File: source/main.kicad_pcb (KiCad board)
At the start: 4 copper layers, 45 x 20 mm, 34 parts, among them J1 SFPEdgeConnector, U1 SNx4LVC541A, U2 EEPROM, U3 LDO 3.3V 250mA Vin max 4.75V 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, U4 CBM9002A_56ILG

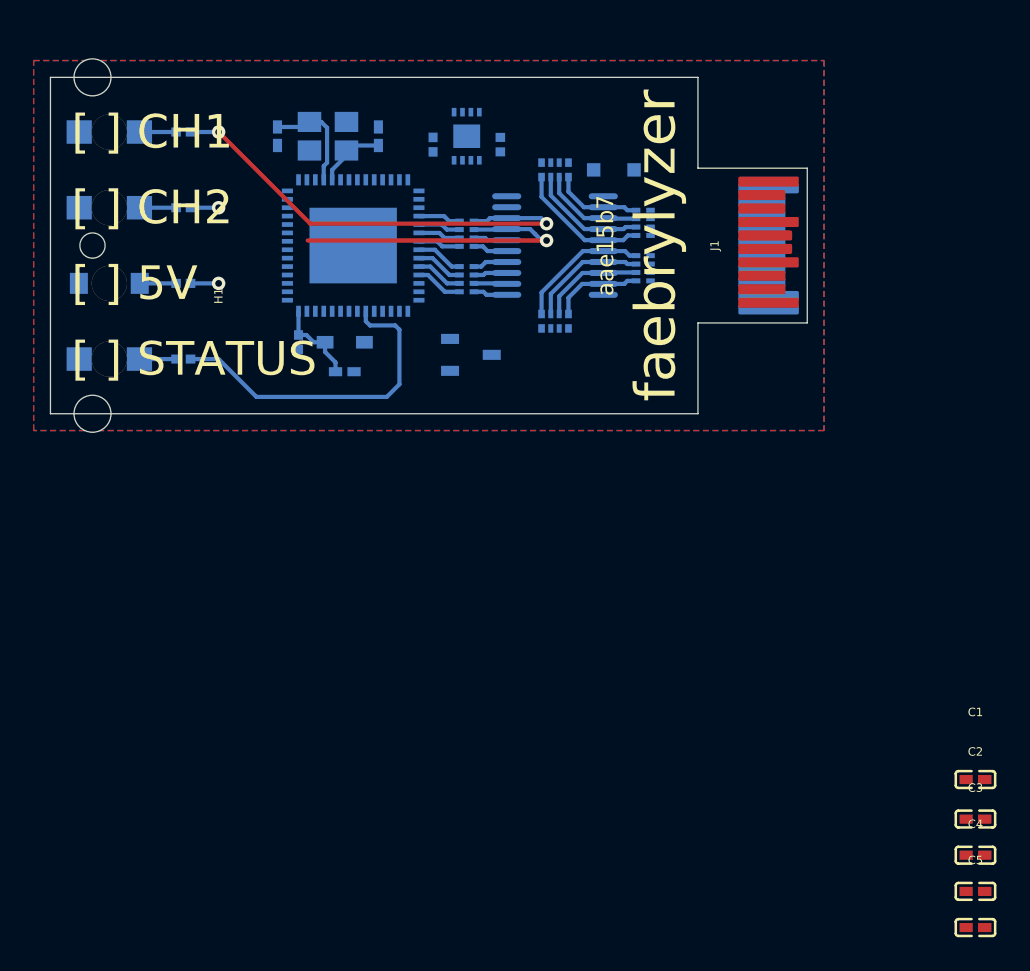
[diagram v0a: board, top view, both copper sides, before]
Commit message: Add: routing and finilize placement
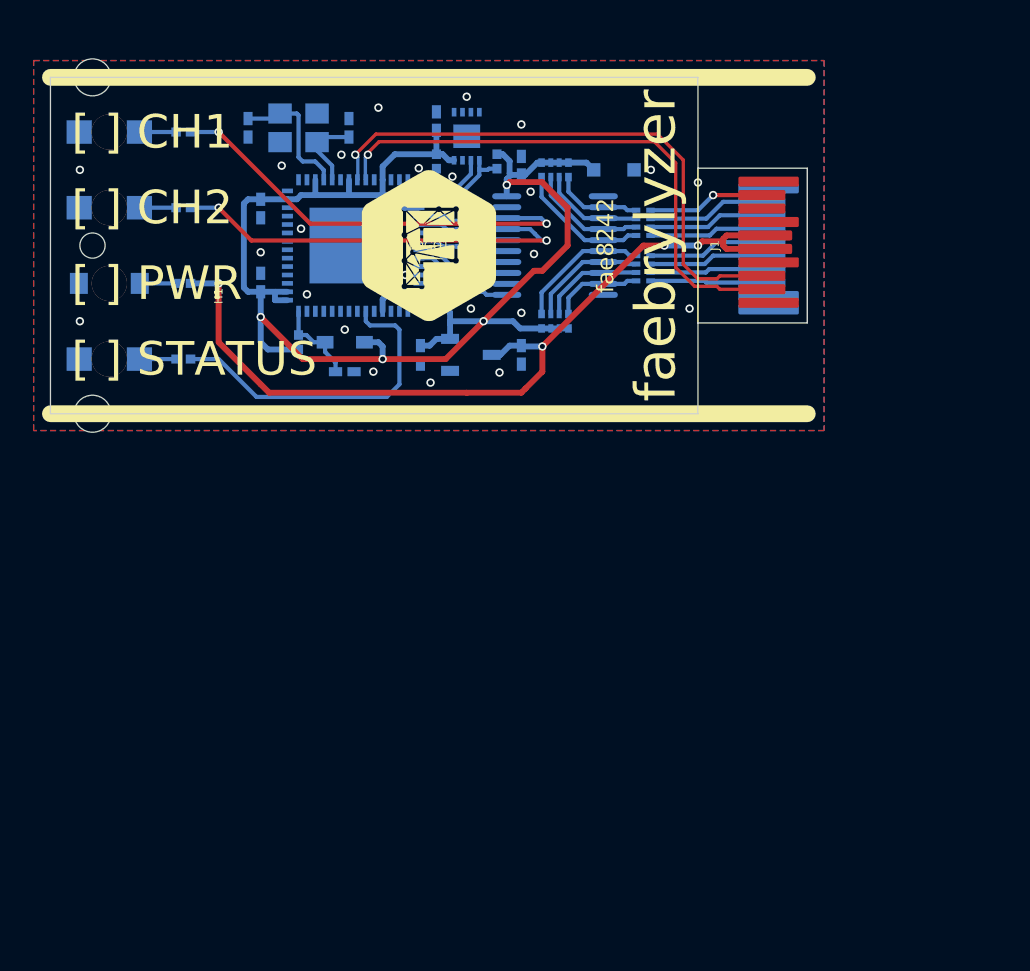
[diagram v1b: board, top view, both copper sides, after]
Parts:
- added C9: 2.2µF ±20% 6.3V X5R, lcsc:C0402, B.Cu at (28.0, 5.25)
- added LOGO1: faebrykLogo, custom:faebryk_logo, F.Cu at (22.5, 10.0)
- C1, C2, C3, C4, C5: moved to B.Cu
- moved C4 58.8 mm to (12.5, 7.80), turned to -90 degrees
- moved C5 57.2 mm to (12.5, 12.2), turned to 90 degrees
- moved C1 50.6 mm to (22.9, 2.60), turned to 90 degrees
- moved C3 44.4 mm to (22.0, 16.5), turned to -90 degrees
- moved C2 38.6 mm to (28.0, 16.5), turned to -90 degrees
- moved C6 1.82 mm to (17.8, 3.00)
- moved XTAL1 1.82 mm to (14.8, 3.00)
- moved C7 1.82 mm to (11.8, 3.00)
- moved R3 1.02 mm to (22.9, 5.00)
- moved R4 1.02 mm to (26.6, 5.00)
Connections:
- J1 pad 12: usb_n -> usb_N
- J1 pad 13: usb_p -> usb_P
- J1 pad 19: J1-19 -> ch_0
- J1 pad 2: ch_0 -> ch_1
- J1 pad 3: ch_1 -> ch_2
- J1 pad 4: ch_2 -> ch_3
- J1 pad 5: ch_3 -> ch_4
- J1 pad 6: ch_4 -> ch_5
- J1 pad 7: ch_5 -> ch_6
- J1 pad 8: ch_6 -> ch_7
- J1 pad 9: ch_7 -> J1-9
- U4 pad 57: U4-57 -> gnd
- U4 pad 8: U4-8 -> usb_P
- U4 pad 9: U4-9 -> usb_N
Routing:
- net 3v3: track 0.00 -> 90.7 mm, vias 0 -> 4
- net vbus: track 1.67 -> 46.6 mm, vias 1 -> 4
- net usb_P: track 0.00 -> 32.1 mm, vias 0 -> 1
- net usb_N: track 0.00 -> 31.2 mm, vias 0 -> 1
- net sda: track 0.00 -> 6.15 mm
- net buffer_out_1: track 20.5 -> 26.6 mm
- net scl: track 0.00 -> 5.66 mm
- net ch_1: track 0.00 -> 5.63 mm
- net ch_0: track 0.00 -> 5.59 mm, vias 0 -> 1
- net ch_4: track 0.00 -> 5.55 mm
- net ch_2: track 0.00 -> 5.51 mm
- net ch_5: track 0.00 -> 5.43 mm
- net ch_3: track 0.00 -> 5.39 mm
- net ch_6: track 0.00 -> 5.30 mm
- net ch_7: track 0.00 -> 5.26 mm
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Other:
- board text added: "[ ] PWR"
- board text added: "fae8242"
- board text removed: "[ ] 5V"
- board text removed: "aae15b7"

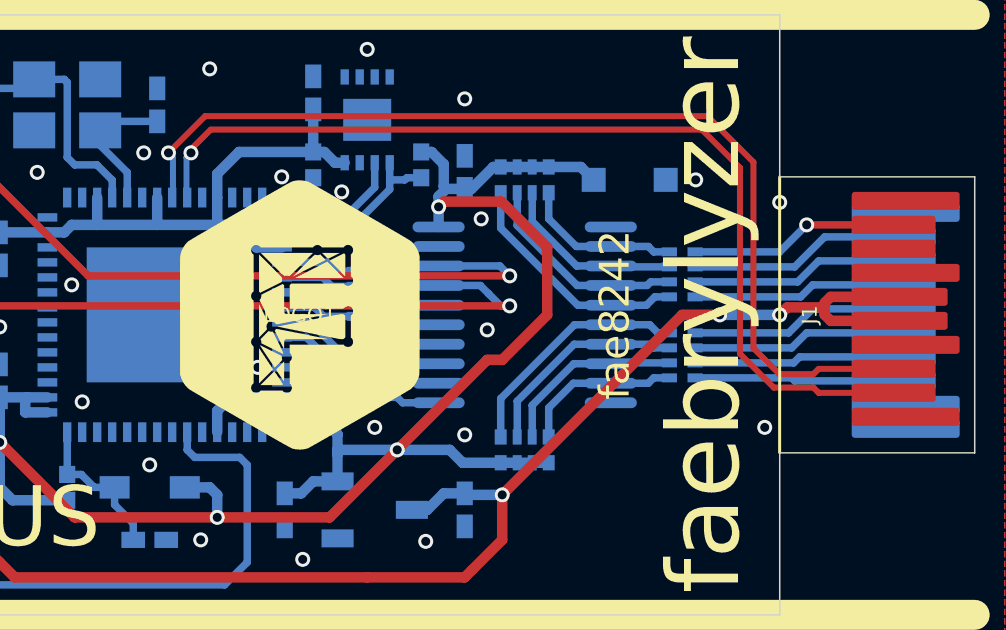
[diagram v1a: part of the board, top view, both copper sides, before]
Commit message: Add: manufacturing arifacts
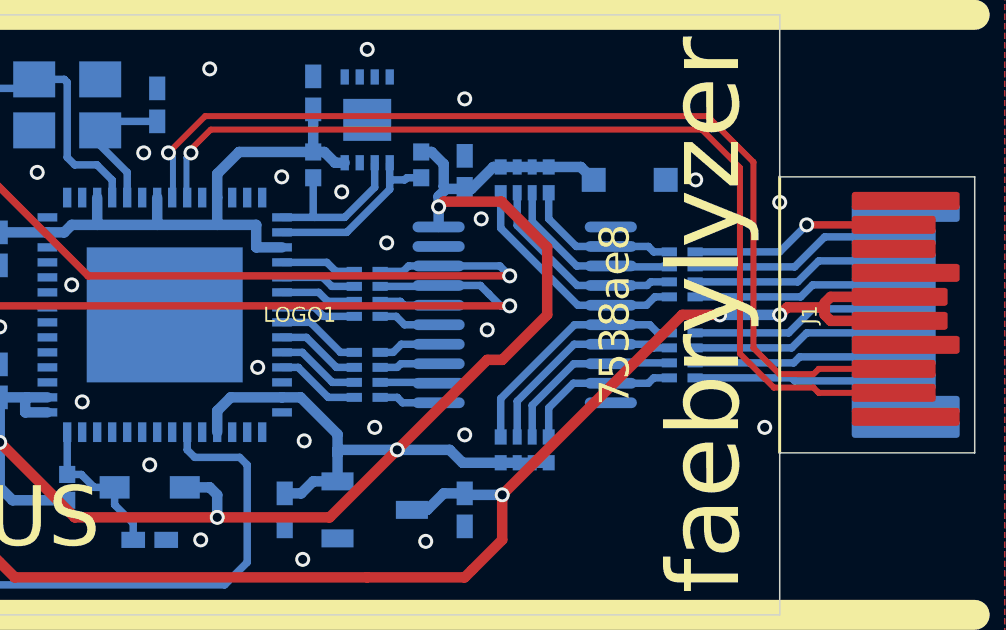
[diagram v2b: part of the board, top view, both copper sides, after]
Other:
- board text added: "7538ae8"
- board text removed: "fae8242"

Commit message: Update to fabll
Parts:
- removed H1: MountingSlot, custom:MountingSlot
- added D7: TVS, lcsc:SOD-323_L1.8-W1.3-LS2.5-BI, B.Cu at (33.5, 13.5)
- C1, C2, C3, C4, C5, C9: value 2.2µF ±20% 6.3V X5R -> 15pF 50V C0G
- U3: value LDO 3.3V 250mA Vin max 4.75V - 5.25V Iq -> LDO 3.3V 250mA Vin max 5V Iq
- XTAL1: footprint lcsc:CRYSTAL-SMD_4P-L3.2-W2.5-BL -> lcsc:CRYSTAL-SMD_4P-L2.0-W1.6-BL-A
- moved C5 5.45 mm to (12.5, 6.75), turned to 270 degrees
- moved C4 3.45 mm to (12.5, 11.2), turned to 90 degrees
- moved C7 2.93 mm to (14.5, 2.00)
- moved LOGO1 2.69 mm to (20.0, 9.00)
- moved XTAL1 2.02 mm to (16.5, 2.00)
- moved C6 1.25 mm to (18.5, 2.00)
- moved J1 1.00 mm to (45.0, 9.00)
- moved C2 1.00 mm to (28.0, 15.5)
- moved C3 1.00 mm to (22.0, 15.5)
- moved C8 1.00 mm to (17.5, 16.5)
- moved C9 1.00 mm to (28.0, 4.25)
- moved D1 1.00 mm to (3.50, 2.25)
- moved D2 1.00 mm to (3.50, 6.75)
- moved D4 1.00 mm to (17.5, 14.8)
- moved D5 1.00 mm to (3.50, 11.2)
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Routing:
- net vbus: track 46.6 -> 50.2 mm
- net C7-1-U4-4-XTAL1-3: track 8.06 -> 5.50 mm
- net R23-2-U4-34: track 19.7 -> 18.8 mm
- net scl: track 5.66 -> 4.91 mm
- net gnd: vias 26 -> 24
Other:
- board size 45 x 20 mm -> 45 x 18 mm
- board text added: "######"
- board text added: "9ac6f78"
- board text removed: "7538ae8"

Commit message: Fix constants; Run
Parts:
- removed R13: 3.3kΩ, lcsc:R0402
- added H1: MountingSlot, custom:MountingSlot, F.Cu at (0.00, 9.00)
- added R9: 100Ω, lcsc:R0402, B.Cu at (14.8, 14.8)
- D3, D7: value TVS -> (none)
- D4: value Diode -> 1.3V; footprint lcsc:SOD-323_L1.8-W1.3-LS2.5-RD -> lcsc:SOD-123FL_L2.8-W1.8-LS3.7-RD
- R1, R2: value 200Ω -> 100Ω
- R3, R4: value 3.3kΩ -> 100Ω
- U3: value LDO 3.3V 250mA Vin max 5V Iq -> LDO 3.3V 237.5mA - 262.5mA Vin max 5V Iq
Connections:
- net C8-1-D4-2-R13-1-U4-42 renamed C8-1-D4-2-R9-1-U4-42
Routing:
- net usb_P: track 32.1 -> 0.00 mm, vias 1 -> 0
- net (no net): track 0.00 -> 32.1 mm, vias 1 -> 2
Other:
- board outline removed
- board text added: "cce994c"
- board text removed: "9ac6f78"
